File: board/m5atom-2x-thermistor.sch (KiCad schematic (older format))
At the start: 2 parts, among them U1 M5_Atom_3.96Plug, U2 ADS1115IDGS

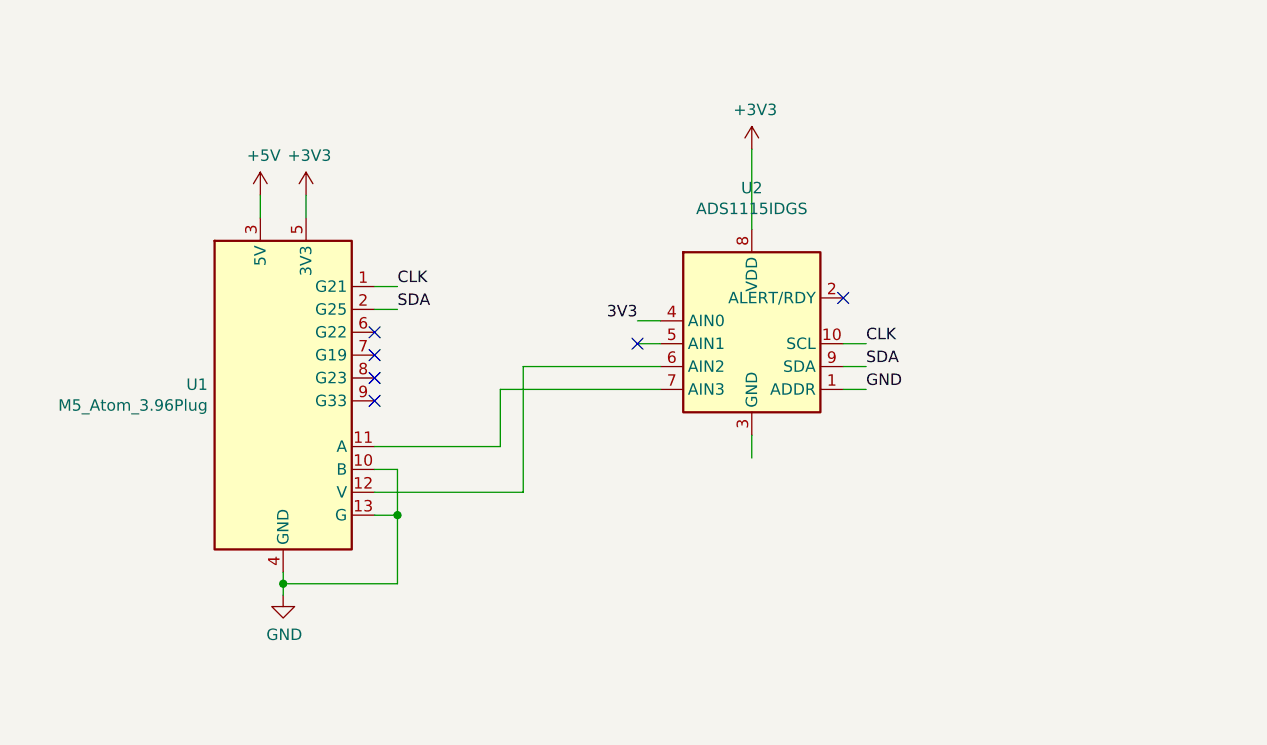
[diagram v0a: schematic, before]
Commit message: New simple board, introducing mess in submodule...
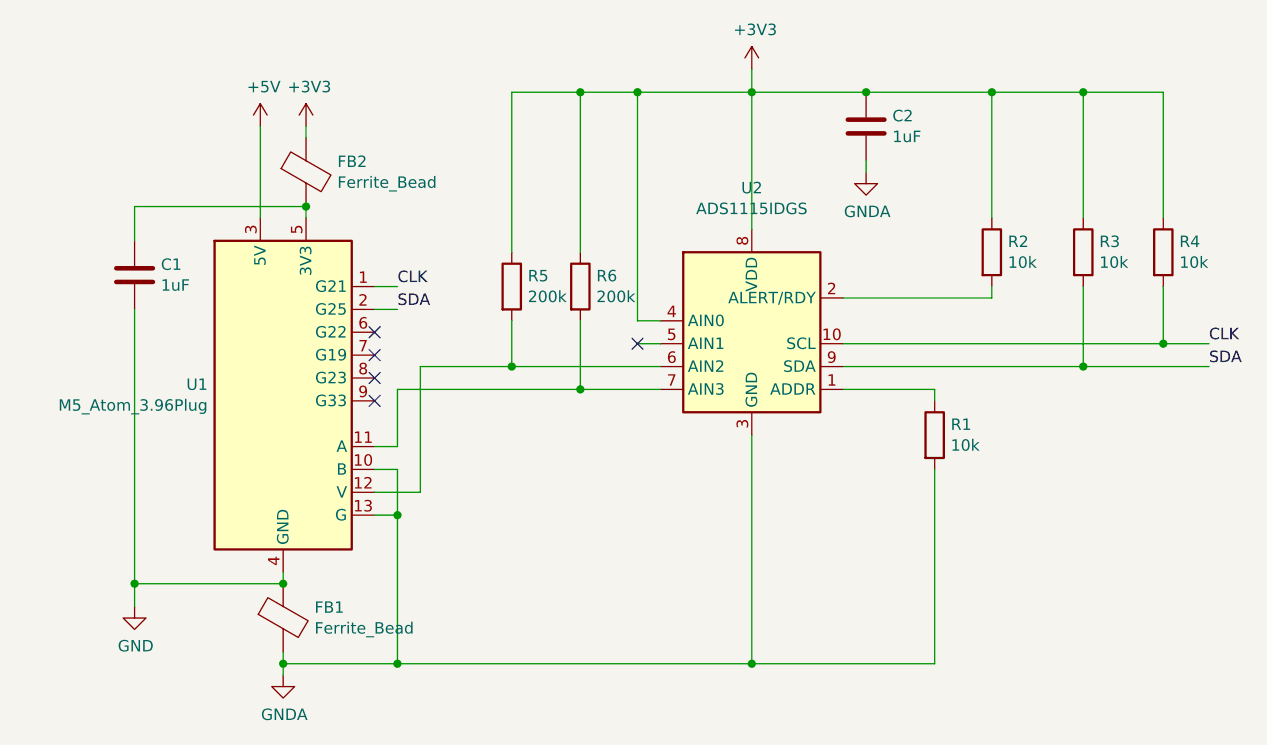
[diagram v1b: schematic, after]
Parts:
- added C1, C2: 1uF, Capacitor_SMD:C_0805_2012Metric, symbol Device:C
- added FB1, FB2: Ferrite_Bead, Resistor_SMD:R_0805_2012Metric, symbol Device:Ferrite_Bead
- added R1, R2, R3, R4: 10k, Resistor_SMD:R_0805_2012Metric, symbol Device:R
- added R5, R6: 200k, Resistor_THT:R_Axial_DIN0204_L3.6mm_D1.6mm_P2.54mm_Vertical, symbol Device:R
- U1: JLCPCB BOM (none) -> 0
- U2: LCSC Part (none) -> C37593
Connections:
- net labels added: GNDA
- net labels removed: 3V3
- wire segments 24 -> 60
- no-connect marks 6 -> 5
